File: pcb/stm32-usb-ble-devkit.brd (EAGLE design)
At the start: 90 x 50 mm, 102 parts, among them CN1 USB-MICROB-2TABS, CN2 USB-C-2.0-FEMALE, CN3 USB-C-2.0-FEMALE, Q2 AO3402, Q4 AO3401, U1 STM32F103-48LQFP, U2 STM32F205-64, U3 TUSB320, U4 TUSB320, U5 HOLYIOT-17051-NRF51822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

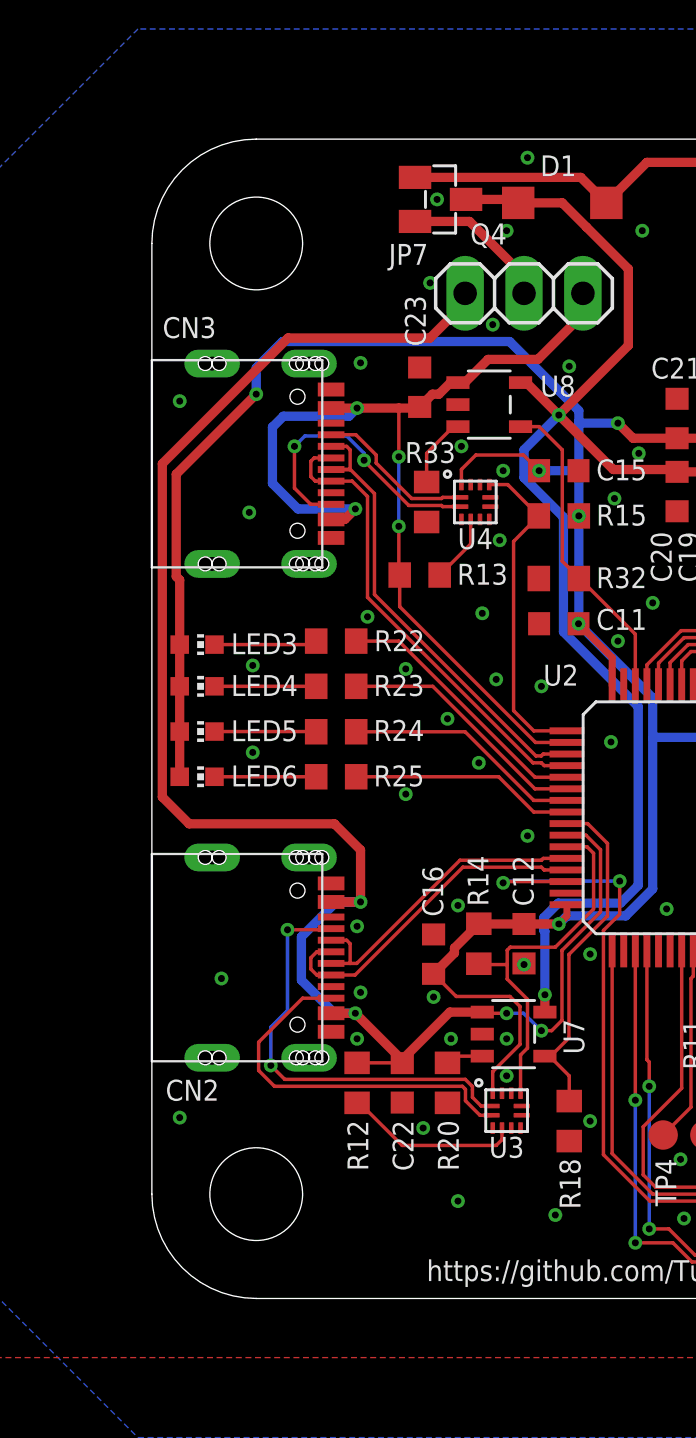
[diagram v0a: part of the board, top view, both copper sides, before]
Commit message: pcb: Slightly shifted USB-HS up
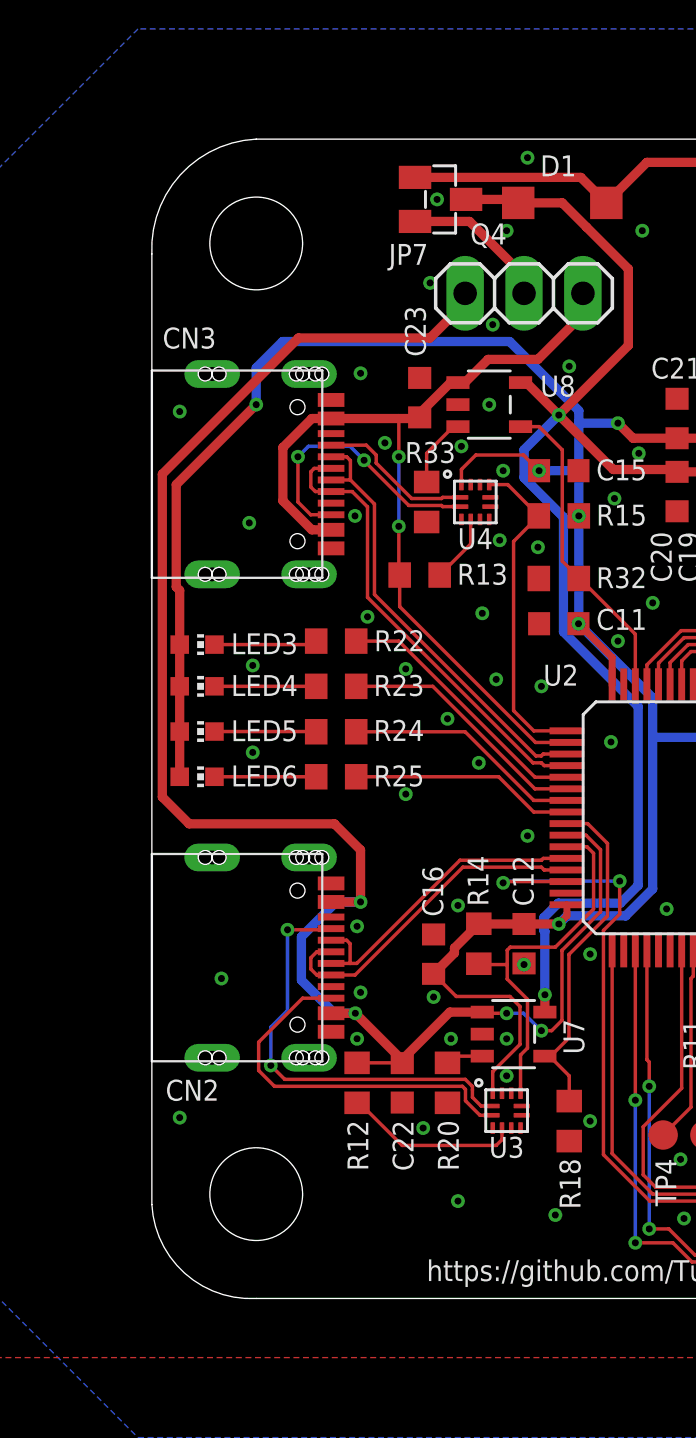
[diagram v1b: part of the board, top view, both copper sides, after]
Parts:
- moved CN3 0.45 mm to (0.00, 35.5)
- moved C23 0.45 mm to (11.6, 38.9)
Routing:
- net USB_HS_VBUS: track 43.3 -> 39.0 mm, vias 4 -> 2
- net USB_HS_N: track 19.9 -> 19.2 mm
- net USB_HS_CC2: track 12.5 -> 11.9 mm
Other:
- outline, holes or cut-outs redrawn

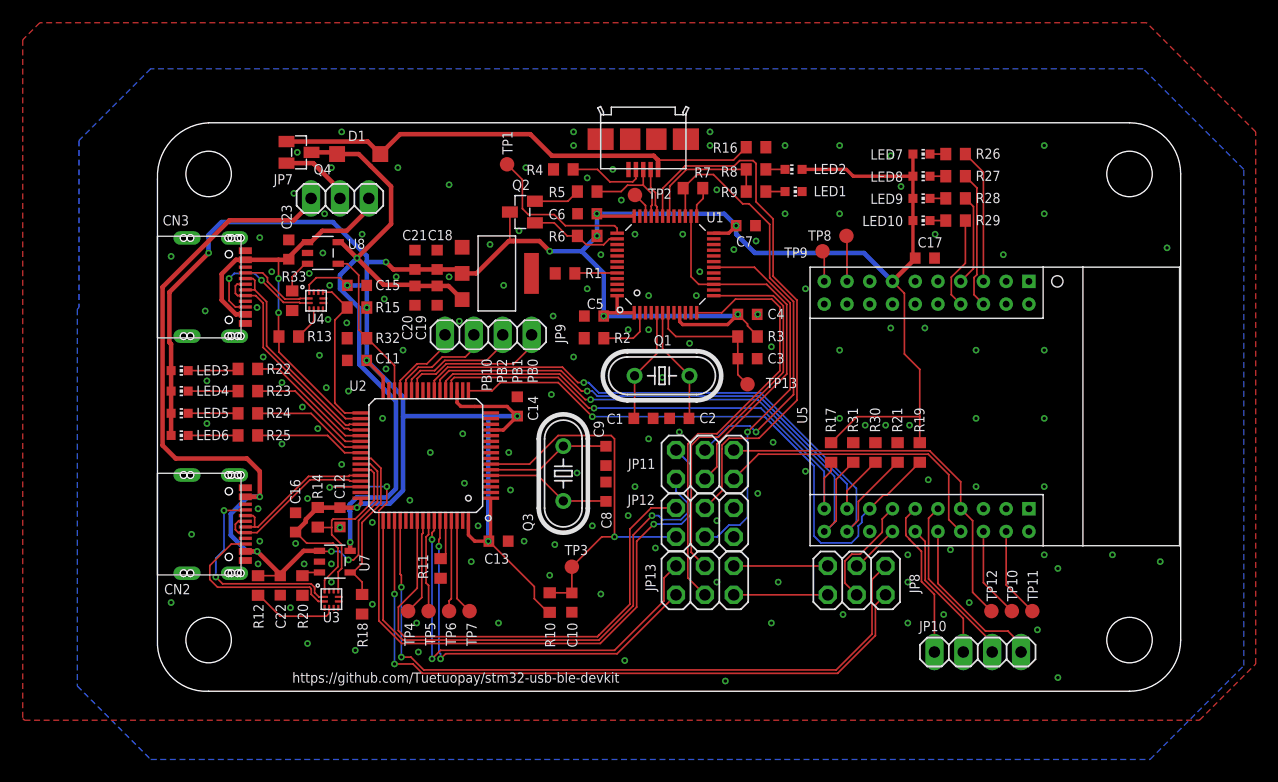
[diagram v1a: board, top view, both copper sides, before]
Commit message: pcb: Switch headers to round pads
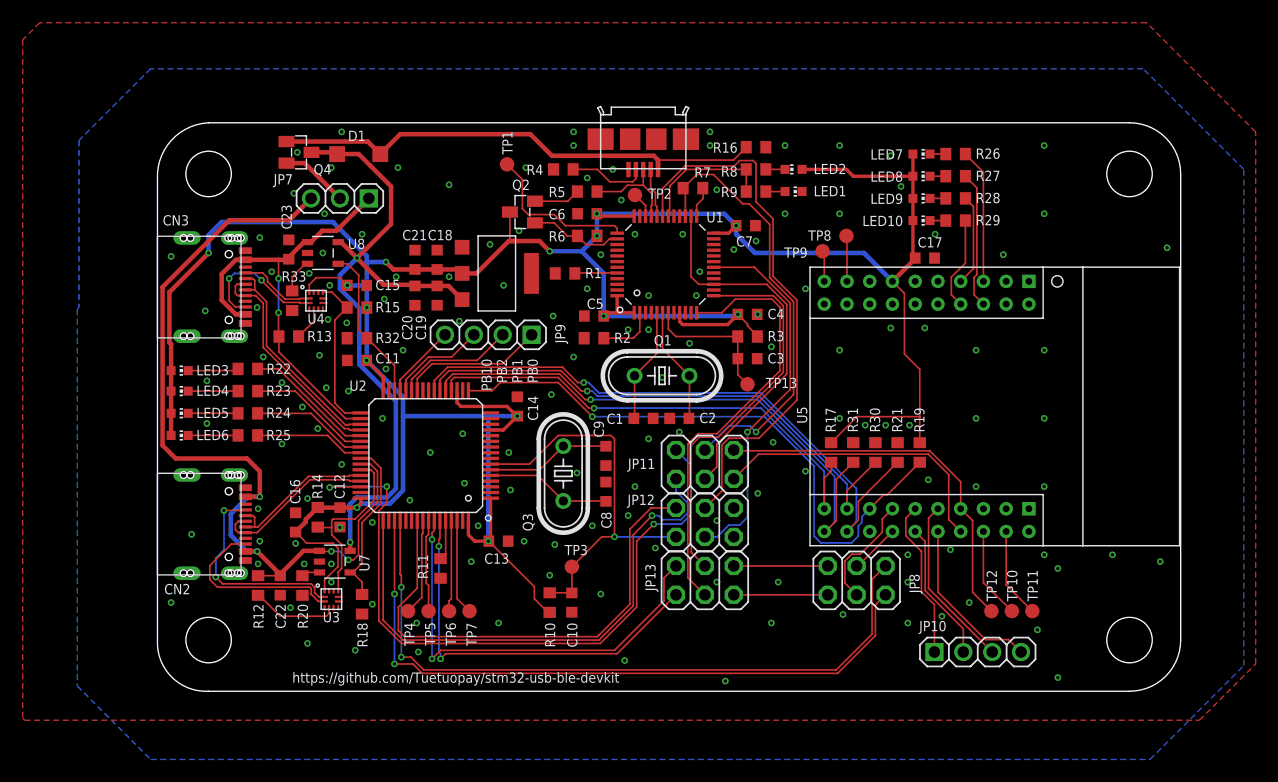
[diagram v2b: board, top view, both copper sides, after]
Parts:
- JP10, JP9: device pinhead:1X04 -> tuetuopay:1X04
- JP7: device pinhead:1X03 -> tuetuopay:1X03
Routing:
- net STM_DBG_PIN2: track 9.29 -> 8.59 mm
- net STM_DBG_PIN0: track 13.3 -> 12.7 mm
- net USB_HS_VBUS: track 39.0 -> 38.5 mm

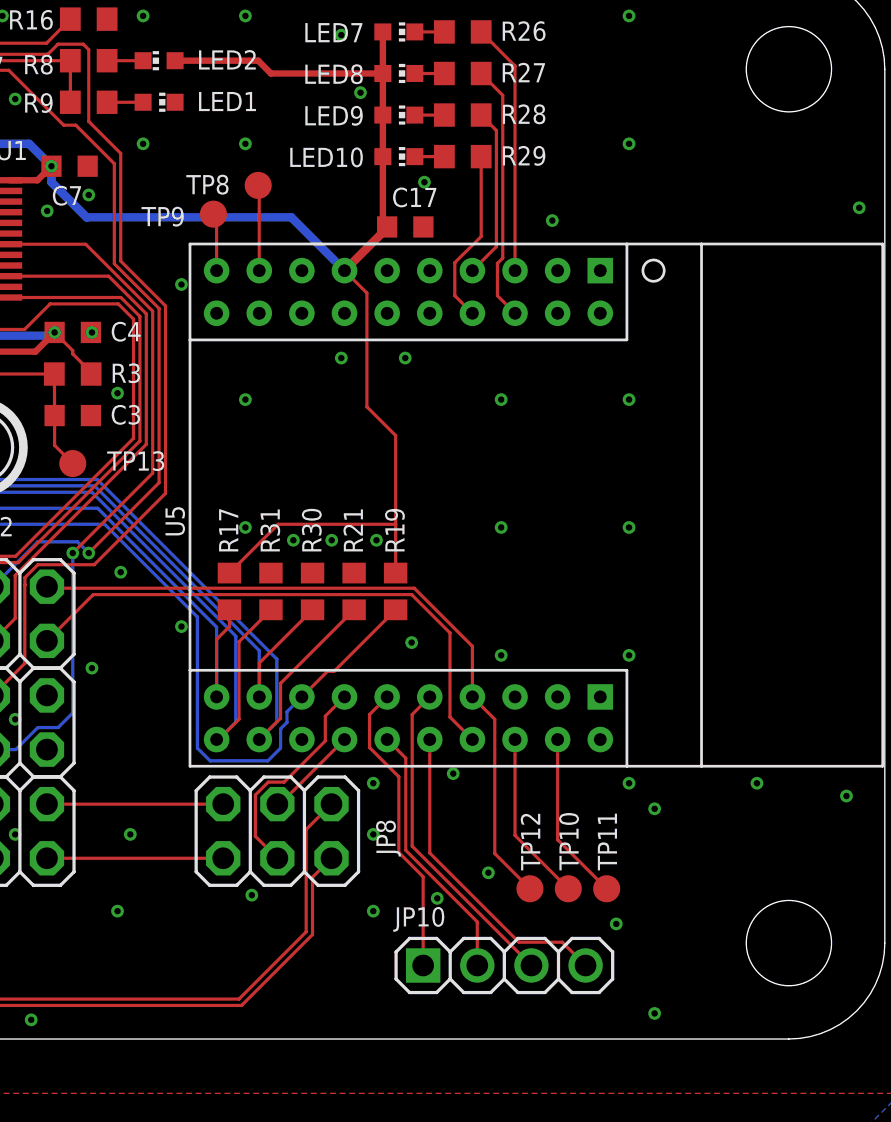
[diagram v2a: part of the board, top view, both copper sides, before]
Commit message: pcb: Moved all nRF TP to the same side
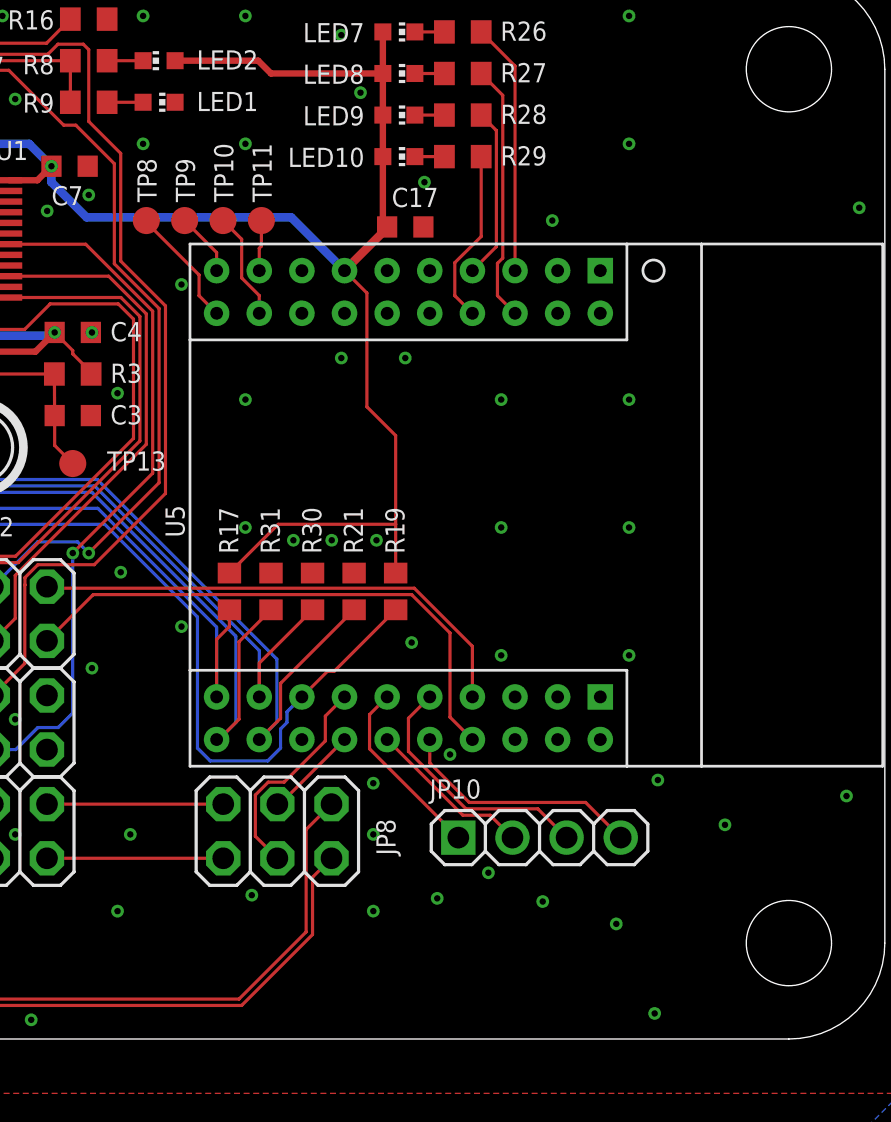
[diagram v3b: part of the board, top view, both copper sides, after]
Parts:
- removed TP12: PTR1B1,27, testpad:B1,27
- moved TP10 35.3 mm to (59.0, 38.4)
- moved TP11 35.3 mm to (60.8, 38.4)
- moved JP10 6.22 mm to (73.8, 9.45)
- moved TP8 5.50 mm to (55.4, 38.4), turned to 270 degrees
- moved TP9 1.38 mm to (57.1, 38.4), turned to 270 degrees
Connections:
- net NRF_DBG_TP_0: now also U5.11; no longer U5.9
- net NRF_DBG_TP_2: now also U5.12; no longer U5.38
- net NRF_DBG_TP_3: now also U5.9; no longer U5.39
- net NRF_SWDIO: no longer TP12.TP
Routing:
- net NRF_SWDIO: track 33.7 -> 23.7 mm
- net NRF_DBG_TP_3: track 7.95 -> 2.39 mm
- net NRF_DBG_PIN_0: track 14.0 -> 8.67 mm
- net NRF_DBG_PIN_1: track 12.4 -> 7.79 mm
- net NRF_DBG_PIN_3: track 14.8 -> 11.5 mm
- net NRF_DBG_PIN_2: track 15.3 -> 12.1 mm
- net NRF_DBG_TP_2: track 8.04 -> 5.05 mm
- net NRF_DBG_TP_0: track 4.02 -> 5.72 mm

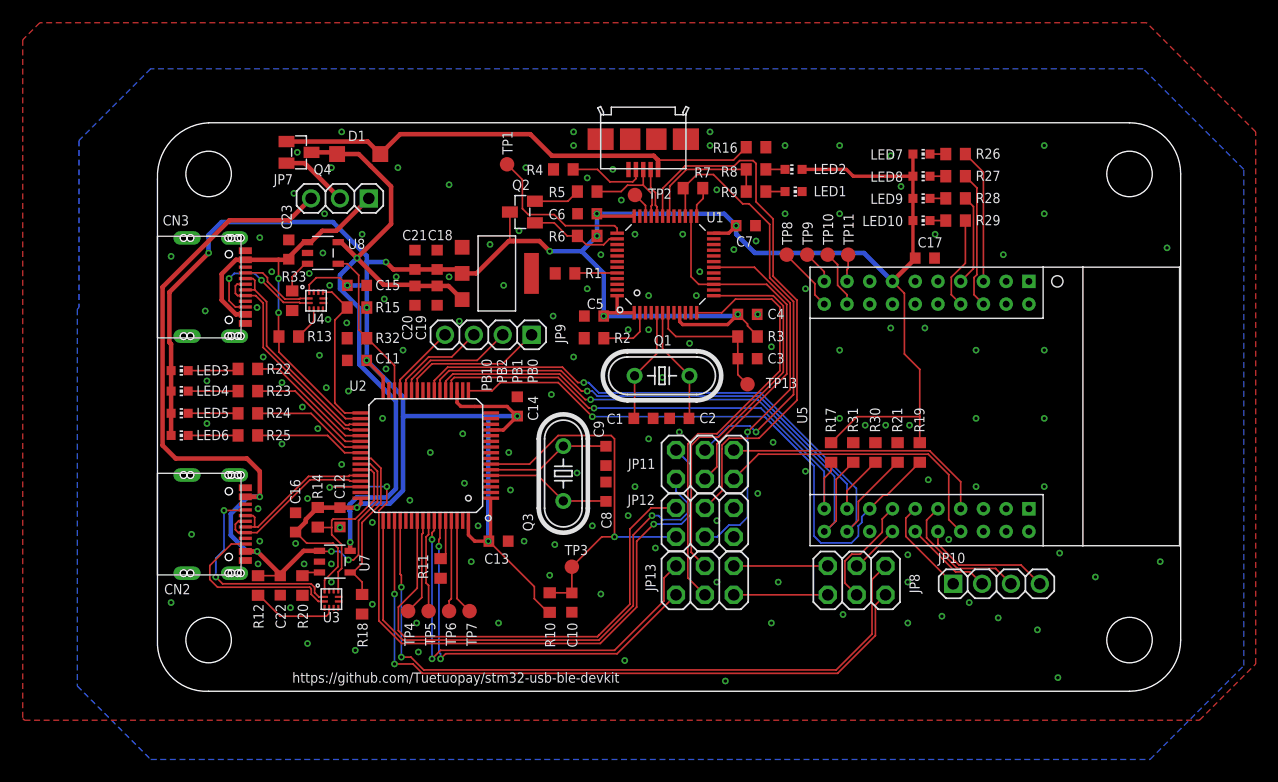
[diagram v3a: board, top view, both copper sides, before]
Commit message: pcb: Add SPI header
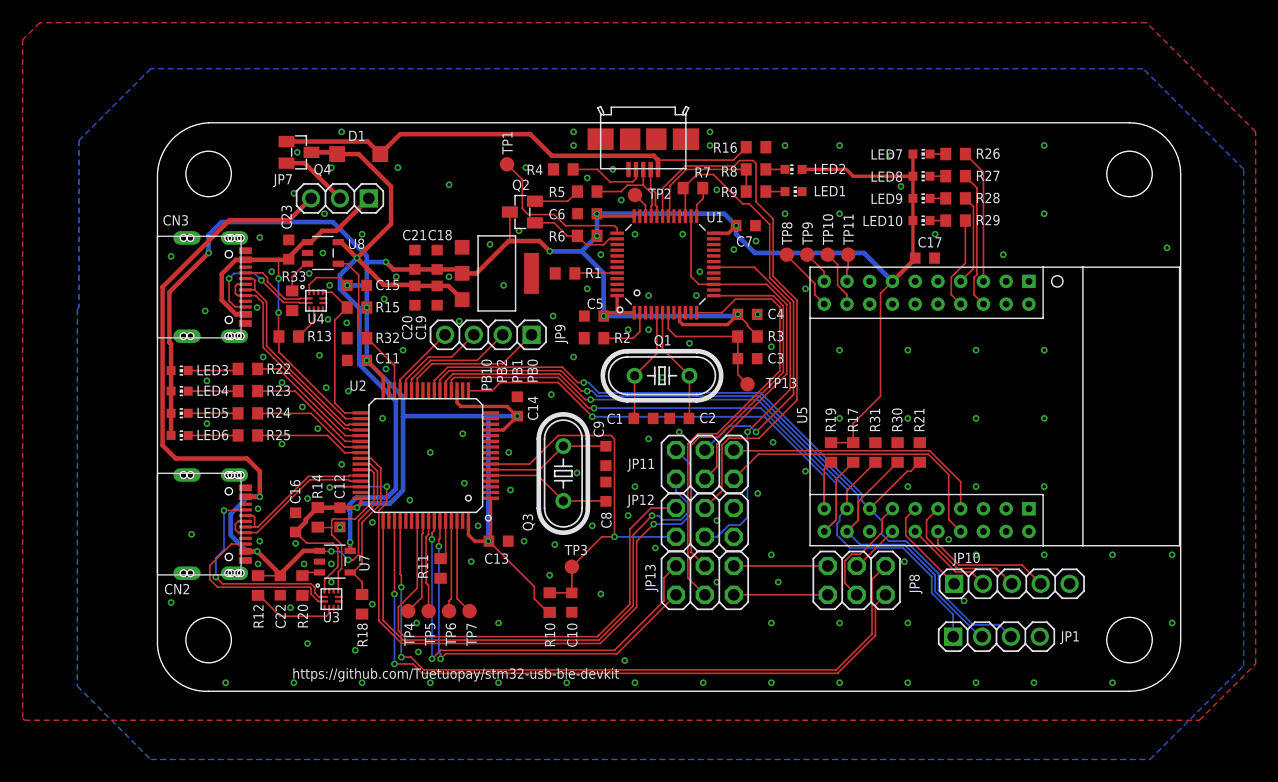
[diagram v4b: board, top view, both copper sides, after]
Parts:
- added JP1: (no value), tuetuopay:1X04
- JP10: device tuetuopay:1X04 -> tuetuopay:1X05
- moved R19 7.80 mm to (59.2, 21.0)
- moved R17 1.95 mm to (61.2, 21.0)
- moved R21 1.95 mm to (67.0, 21.0)
- moved R30 1.95 mm to (65.1, 21.0)
- moved R31 1.95 mm to (63.1, 21.0)
- moved JP10 1.35 mm to (75.2, 9.45)
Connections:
- net GND: now also JP1.4, JP10.5
- net SPI_CS: now also U5.30; no longer U5.28
- net SPI_IRQ: now also U5.31; no longer U5.30
- net SPI_MISO: now also JP1.2, U5.32; no longer U5.29
- net SPI_MOSI: now also JP1.3, U5.28; no longer U5.32
- net SPI_SCK: now also JP1.1, U5.29; no longer U5.31
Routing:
- net SPI_MISO: track 48.5 -> 70.7 mm
- net SPI_MOSI: track 55.0 -> 69.9 mm
- net SPI_SCK: track 51.5 -> 66.0 mm
- net SPI_CS: track 53.2 -> 42.2 mm
- net +3V3: track 273.3 -> 267.0 mm
- net SPI_IRQ: track 44.9 -> 50.5 mm
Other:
- board text added: "SCK MISO MOSI GND"
